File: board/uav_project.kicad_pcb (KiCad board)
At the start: 2 copper layers, 80 x 59.9 mm, 79 parts, among them IC1 RT9193-33GB, IC2 NJG1130KA1-TE1, J1 Conn_01x07, J3 Bat IN Terminal, J4 Bat OUT Terminal, J5 Conn_Coaxial, Q1 PMOS, U1 INA226, U2 AMS1117-3.3, U3 INA226, U4 LM2596S-5, U5 PCA9685PW, U6 NEO-M7N, U7 WT901B

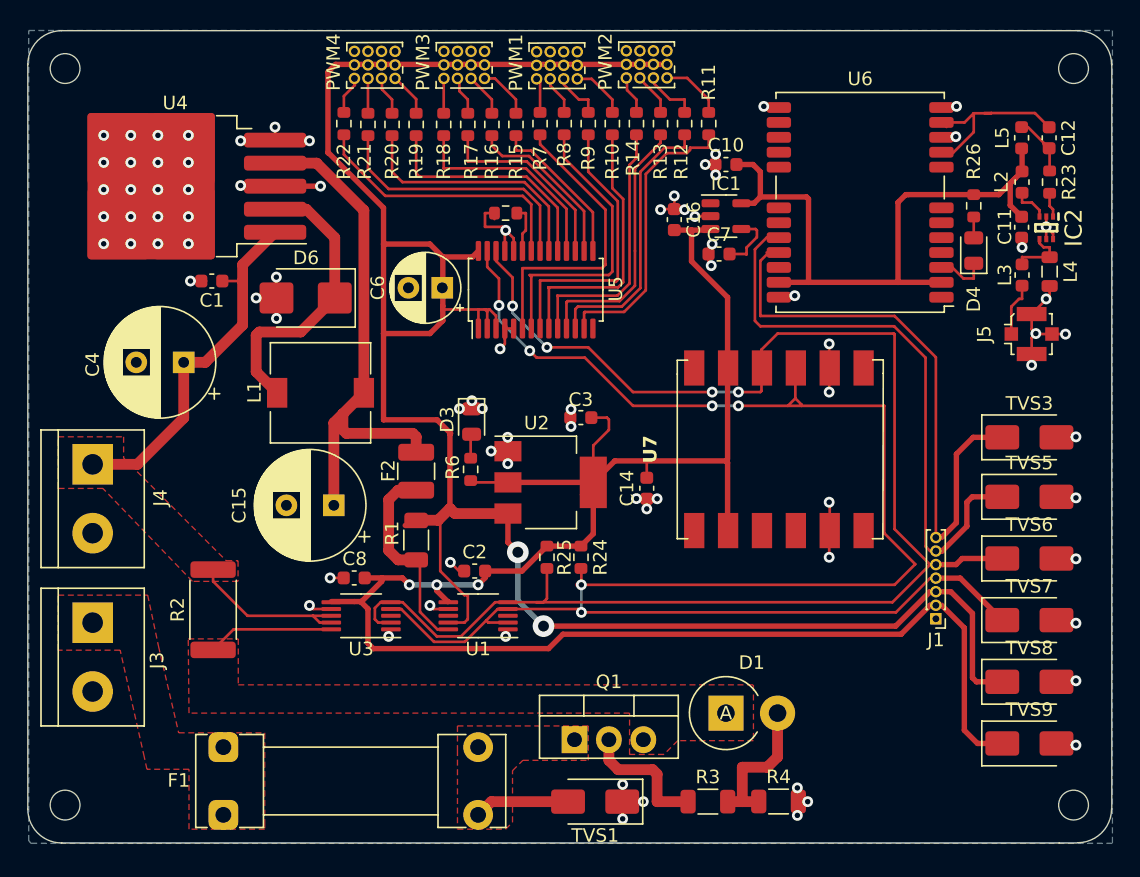
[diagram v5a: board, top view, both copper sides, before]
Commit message: Cleanup on drone side, to make code more bearable and simple
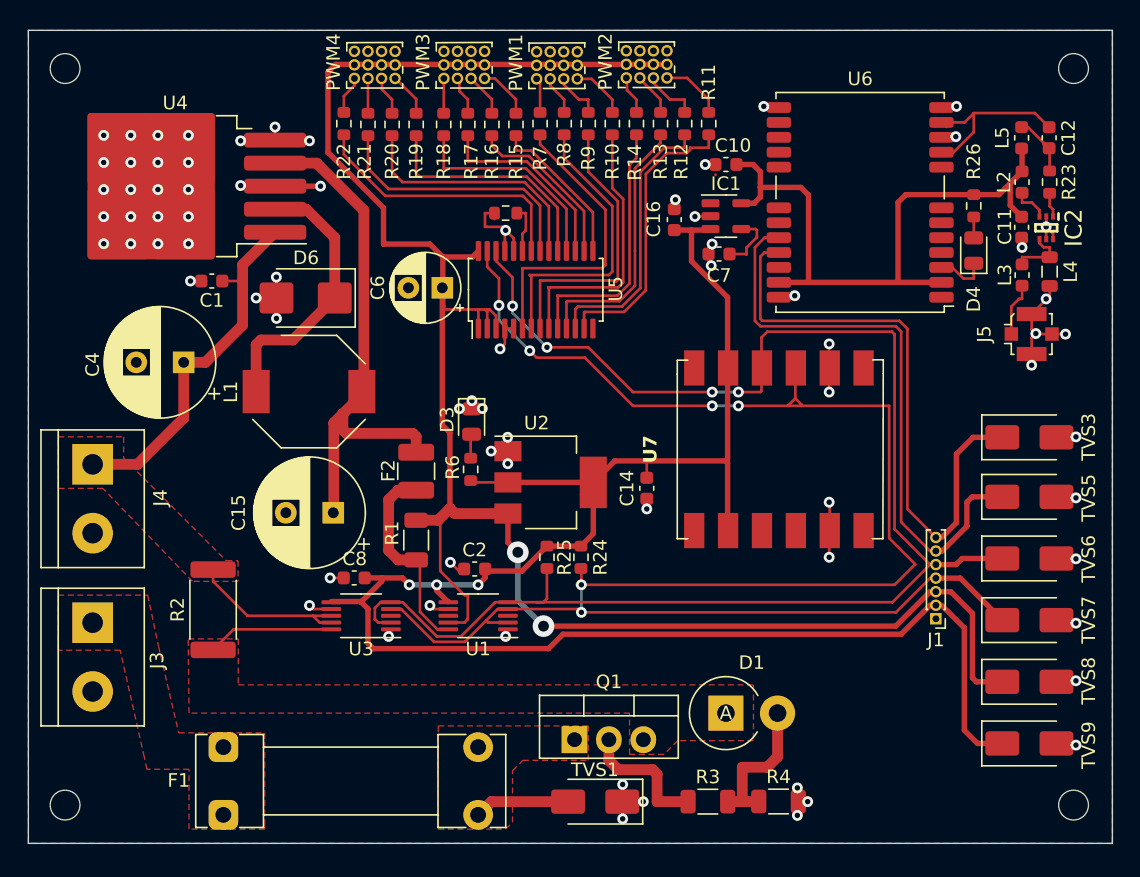
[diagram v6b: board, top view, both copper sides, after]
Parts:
- removed C3: 100n, Capacitor_SMD:C_0603_1608Metric
- L1: footprint Inductor_SMD:L_7.3x7.3_H3.5 -> Inductor_SMD:L_Bourns-SRU8043
- moved L1 0.85 mm to (110.7, 91.7)
- moved C15 0.55 mm to (112.5, 100.6)
- moved C2 0.15 mm to (122.9, 104.8)
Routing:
- net +5V: track 164.7 -> 150.3 mm
- net +3V3: track 145.5 -> 139.0 mm
- net GND: track 93.3 -> 86.9 mm, vias 83 -> 75
- net Net-(D6-K): track 21.6 -> 18.9 mm
- net SLC: track 113.1 -> 113.8 mm
- net RX: track 44.6 -> 44.0 mm
- net /GPS module/RF_IN: track 13.6 -> 13.1 mm
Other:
- board size 80 x 59.9 mm -> 80 x 60 mm

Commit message: Minor improvement to the board
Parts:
- added L6: 18n, Inductor_SMD:L_0805_2012Metric, F.Cu at (161.5, 74.4)
- added R27: 10, Resistor_SMD:R_0603_1608Metric, F.Cu at (159.8, 74.7)
- moved C16 2.58 mm to (137.4, 81.5), turned to 0 degrees
- moved C10 1.92 mm to (143.3, 74.2), turned to -90 degrees
- moved C11 1.29 mm to (164.6, 79.5)
- moved C12 1.29 mm to (166.6, 72.9)
- moved IC2 1.29 mm to (166.4, 79.5)
- moved J5 1.29 mm to (165.3, 87.4)
- moved L2 1.29 mm to (164.6, 76.2)
- moved L3 1.29 mm to (164.6, 83.0)
- moved L5 1.29 mm to (164.6, 72.9)
- moved L4 1.29 mm to (166.7, 82.8), turned to 90 degrees
- moved R23 1.29 mm to (166.7, 76.2)
- moved C1 1.11 mm to (104.6, 83.6)
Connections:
- L4 pad 1: Net-(IC2-RF_IN) -> GND
- L4 pad 2: GND -> Net-(IC2-RF_IN)
- U6 pad 9: /GPS module/RF_IN -> /GPS module/VCC_RF
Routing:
- net SDA: track 133.1 -> 109.7 mm, vias 6 -> 7
- net Net-(U4-FB): track 38.6 -> 41.9 mm
- net /GPS module/VCC_RF: track 0.00 -> 2.44 mm
- net Net-(L6-Pad1): track 0.00 -> 1.78 mm
- net /Servo driver/PWM1: track 21.8 -> 20.0 mm
- net /Servo driver/PWM2: track 21.0 -> 19.3 mm
- net /Servo driver/PWM0: track 22.3 -> 20.6 mm
- net /Power managment/5V SENSE IN: track 15.0 -> 16.5 mm
- net /GPS module/+3V3 LN: track 60.8 -> 62.3 mm
- net /Power managment/BAT SENSE OUT: track 39.3 -> 37.8 mm
- net Net-(D6-K): track 18.9 -> 20.4 mm
- net /Servo driver/PWM3: track 19.9 -> 18.6 mm
- net GND: track 86.9 -> 85.8 mm, vias 75 -> 76
- net /Servo driver/PWM4: track 19.3 -> 18.3 mm
- net +3V3: track 139.0 -> 139.9 mm
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
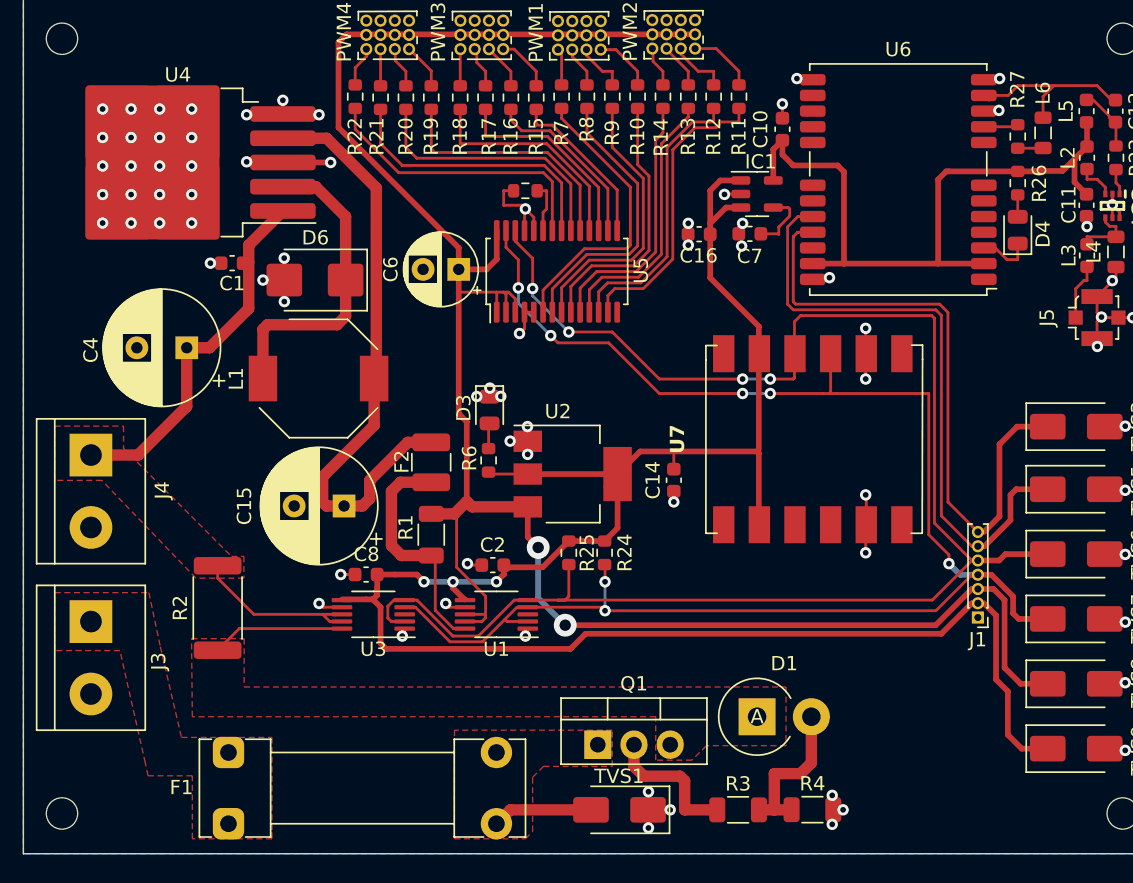
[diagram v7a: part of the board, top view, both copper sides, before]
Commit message: Compilation on bananpi works
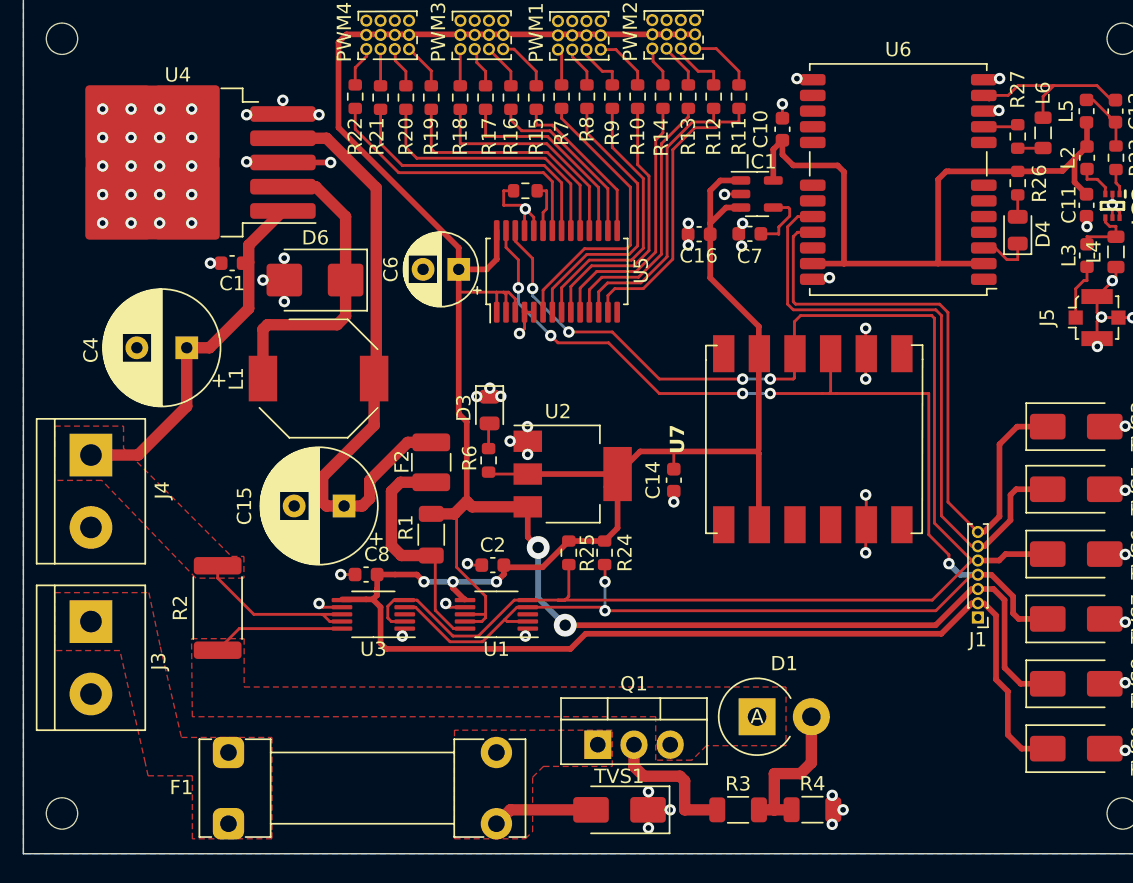
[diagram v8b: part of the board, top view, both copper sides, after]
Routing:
- net /GPS module/+3V3 LN: track 62.3 -> 61.7 mm
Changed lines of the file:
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@@
       (outputformat 1)
       (mirror false)
-      (drillshape 1)
+      (drillshape 0)
       (scaleselection 1)
-      (outputdirectory "")
+      (outputdirectory "1")
     )
   )
@@
     (fp_line (start 3.15 1.6) (end -3.15 1.6)
       (stroke (width 0.1) (type solid)) (layer "F.Fab"))
-    (pad "1" smd roundrect (at -2.9625 0 90) (size 1.225 3.35) (layers "F.Cu" "F.Paste" "F.Mask") (roundrect_rratio 0.204082)
+    (pad "1" smd roundrect (at -2.9625 0 90) (size 1.225 3.35) (layers "F.Cu" "F.Paste" "F.Mask") (roundrect_rratio 0.2040816327)
       (net 31 "/Power managment/BAT SENSE IN") (pintype "passive"))
-    (pad "2" smd roundrect (at 2.9625 0 90) (size 1.225 3.35) (layers "F.Cu" "F.Paste" "F.Mask") (roundrect_rratio 0.204082)
+    (pad "2" smd roundrect (at 2.9625 0 90) (size 1.225 3.35) (layers "F.Cu" "F.Paste" "F.Mask") (roundrect_rratio 0.2040816327)
       (net 30 "/Power managment/BAT SENSE OUT") (pintype "passive"))
     (model "${KICAD6_3DMODEL_DIR}/Resistor_SMD.3dshapes/R_2512_6332Metric.wrl"
@@
     (fp_line (start 5.625 5) (end 4.625 5)
       (stroke (width 0.1) (type solid)) (layer "F.Fab"))
-    (pad "1" smd roundrect (at -7.65 -3.4 180) (size 4.6 1.1) (layers "F.Cu" "F.Paste" "F.Mask") (roundrect_rratio 0.227273)
+    (pad "1" smd roundrect (at -7.65 -3.4 180) (size 4.6 1.1) (layers "F.Cu" "F.Paste" "F.Mask") (roundrect_rratio 0.2272727273)
       (net 30 "/Power managment/BAT SENSE OUT") (pinfunction "VIN") (pintype "power_in"))
-    (pad "2" smd roundrect (at -7.65 -1.7 180) (size 4.6 1.1) (layers "F.Cu" "F.Paste" "F.Mask") (roundrect_rratio 0.227273)
+    (pad "2" smd roundrect (at -7.65 -1.7 180) (size 4.6 1.1) (layers "F.Cu" "F.Paste" "F.Mask") (roundrect_rratio 0.2272727273)
       (net 28 "Net-(D6-K)") (pinfunction "OUT") (pintype "output"))
-    (pad "3" smd roundrect (at -7.65 0 180) (size 4.6 1.1) (layers "F.Cu" "F.Paste" "F.Mask") (roundrect_rratio 0.227273)
+    (pad "3" smd roundrect (at -7.65 0 180) (size 4.6 1.1) (layers "F.Cu" "F.Paste" "F.Mask") (roundrect_rratio 0.2272727273)
       (net 1 "GND") (pinfunction "GND") (pintype "power_in"))
-    (pad "3" smd roundrect (at -0.925 -2.775 180) (size 4.55 5.25) (layers "F.Cu" "F.Paste") (roundrect_rratio 0.054945)
+    (pad "3" smd roundrect (at -0.925 -2.775 180) (size 4.55 5.25) (layers "F.Cu" "F.Paste") (roundrect_rratio 0.05494505495)
       (net 1 "GND") (pinfunction "GND") (pintype "power_in"))
-    (pad "3" smd roundrect (at -0.925 2.775 180) (size 4.55 5.25) (layers "F.Cu" "F.Paste") (roundrect_rratio 0.054945)
+    (pad "3" smd roundrect (at -0.925 2.775 180) (size 4.55 5.25) (layers "F.Cu" "F.Paste") (roundrect_rratio 0.05494505495)
       (net 1 "GND") (pinfunction "GND") (pintype "power_in"))
-    (pad "3" smd roundrect (at 1.5 0 180) (size 9.4 10.8) (layers "F.Cu" "F.Mask") (roundrect_rratio 0.026596)
+    (pad "3" smd roundrect (at 1.5 0 180) (size 9.4 10.8) (layers "F.Cu" "F.Mask") (roundrect_rratio 0.02659595745)
       (net 1 "GND") (pinfunction "GND") (pintype "power_in"))
-    (pad "3" smd roundrect (at 3.925 -2.775 180) (size 4.55 5.25) (layers "F.Cu" "F.Paste") (roundrect_rratio 0.054945)
+    (pad "3" smd roundrect (at 3.925 -2.775 180) (size 4.55 5.25) (layers "F.Cu" "F.Paste") (roundrect_rratio 0.05494505495)
       (net 1 "GND") (pinfunction "GND") (pintype "power_in"))
-    (pad "3" smd roundrect (at 3.925 2.775 180) (size 4.55 5.25) (layers "F.Cu" "F.Paste") (roundrect_rratio 0.054945)
+    (pad "3" smd roundrect (at 3.925 2.775 180) (size 4.55 5.25) (layers "F.Cu" "F.Paste") (roundrect_rratio 0.05494505495)
       (net 1 "GND") (pinfunction "GND") (pintype "power_in"))
-    (pad "4" smd roundrect (at -7.65 1.7 180) (size 4.6 1.1) (layers "F.Cu" "F.Paste" "F.Mask") (roundrect_rratio 0.227273)
+    (pad "4" smd roundrect (at -7.65 1.7 180) (size 4.6 1.1) (layers "F.Cu" "F.Paste" "F.Mask") (roundrect_rratio 0.2272727273)
       (net 3 "Net-(U4-FB)") (pinfunction "FB") (pintype "input"))
-    (pad "5" smd roundrect (at -7.65 3.4 180) (size 4.6 1.1) (layers "F.Cu" "F.Paste" "F.Mask") (roundrect_rratio 0.227273)
+    (pad "5" smd roundrect (at -7.65 3.4 180) (size 4.6 1.1) (layers "F.Cu" "F.Paste" "F.Mask") (roundrect_rratio 0.2272727273)
       (net 1 "GND") (pinfunction "~{ON}/OFF") (pintype "input"))
     (model "${KICAD6_3DMODEL_DIR}/Package_TO_SOT_SMD.3dshapes/TO-263-5_TabPin3.wrl"
@@
     (property "ki_keywords" "cap capacitor")
     (attr smd)
-    (fp_text reference "C8" (at -0.034 1.41) (layer "F.SilkS")
+    (fp_text reference "C8" (at -0.762 1.41) (layer "F.SilkS")
         (effects (font (size 1 1) (thickness 0.15)))
     )
@@
     (fp_line (start 1.6 0.8) (end -1.6 0.8)
       (stroke (width 0.1) (type solid)) (layer "F.Fab"))
-    (pad "1" smd roundrect (at -1.4625 0) (size 1.125 1.75) (layers "F.Cu" "F.Paste" "F.Mask") (roundrect_rratio 0.222222)
+    (pad "1" smd roundrect (at -1.4625 0) (size 1.125 1.75) (layers "F.Cu" "F.Paste" "F.Mask") (roundrect_rratio 0.2222222222)
       (net 41 "Net-(Q1-G)") (pintype "passive"))
-    (pad "2" smd roundrect (at 1.4625 0) (size 1.125 1.75) (layers "F.Cu" "F.Paste" "F.Mask") (roundrect_rratio 0.222222)
+    (pad "2" smd roundrect (at 1.4625 0) (size 1.125 1.75) (layers "F.Cu" "F.Paste" "F.Mask") (roundrect_rratio 0.2222222222)
       (net 25 "Net-(D1-A)") (pintype "passive"))
     (model "${KICAD6_3DMODEL_DIR}/Resistor_SMD.3dshapes/R_1206_3216Metric.wrl"
@@
     (fp_line (start 1.6 0.8) (end -1.6 0.8)
       (stroke (width 0.1) (type solid)) (layer "F.Fab"))
-    (pad "1" smd roundrect (at -1.4625 0) (size 1.125 1.75) (layers "F.Cu" "F.Paste" "F.Mask") (roundrect_rratio 0.222222)
+    (pad "1" smd roundrect (at -1.4625 0) (size 1.125 1.75) (layers "F.Cu" "F.Paste" "F.Mask") (roundrect_rratio 0.2222222222)
       (net 25 "Net-(D1-A)") (pintype "passive"))
-    (pad "2" smd roundrect (at 1.4625 0) (size 1.125 1.75) (layers "F.Cu" "F.Paste" "F.Mask") (roundrect_rratio 0.222222)
+    (pad "2" smd roundrect (at 1.4625 0) (size 1.125 1.75) (layers "F.Cu" "F.Paste" "F.Mask") (roundrect_rratio 0.2222222222)
       (net 1 "GND") (pintype "passive"))
     (model "${KICAD6_3DMODEL_DIR}/Resistor_SMD.3dshapes/R_1206_3216Metric.wrl"
@@
     (fp_line (start 1.6 0.8) (end -1.6 0.8)
       (stroke (width 0.1) (type solid)) (layer "F.Fab"))
-    (pad "1" smd roundrect (at -1.4625 0 90) (size 1.125 1.75) (layers "F.Cu" "F.Paste" "F.Mask") (roundrect_rratio 0.222222)
+    (pad "1" smd roundrect (at -1.4625 0 90) (size 1.125 1.75) (layers "F.Cu" "F.Paste" "F.Mask") (roundrect_rratio 0.2222222222)
       (net 81 "/Power managment/5V SENSE IN") (pintype "passive"))
-    (pad "2" smd roundrect (at 1.4625 0 90) (size 1.125 1.75) (layers "F.Cu" "F.Paste" "F.Mask") (roundrect_rratio 0.222222)
+    (pad "2" smd roundrect (at 1.4625 0 90) (size 1.125 1.75) (layers "F.Cu" "F.Paste" "F.Mask") (roundrect_rratio 0.2222222222)
       (net 4 "+5V") (pintype "passive"))
     (model "${KICAD6_3DMODEL_DIR}/Resistor_SMD.3dshapes/R_1206_3216Metric.wrl"
@@
   (segment (start 138.901 77.761) (end 140.3405 77.761) (width 0.4) (layer "F.Cu") (net 2))
   (segment (start 140.2615 79.74) (end 140.3405 79.661) (width 0.4) (layer "F.Cu") (net 2))
-  (segment (start 114.554 107.188) (end 114.52 107.154) (width 0.4) (layer "F.Cu") (net 2))
   (segment (start 131.69 102.151) (end 130.78 103.061) (width 0.4) (layer "F.Cu") (net 2))
   (segment (start 125.39 98.36) (end 131.69 98.36) (width 0.4) (layer "F.Cu") (net 2))
@@
   (segment (start 157.384 83.595) (end 147.574 83.595) (width 0.4) (layer "F.Cu") (net 6))
   (segment (start 147.574 83.595) (end 145.384 83.595) (width 0.4) (layer "F.Cu") (net 6))
-  (segment (start 161.036 77.124) (end 161.622 77.124) (width 0.4) (layer "F.Cu") (net 6))
   (segment (start 143.256 75.946) (end 144.018 76.708) (width 0.4) (layer "F.Cu") (net 6))
   (segment (start 162.914 77.0945) (end 161.0655 77.0945) (width 0.4) (layer "F.Cu") (net 6))
